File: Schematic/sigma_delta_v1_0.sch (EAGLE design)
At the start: 46 parts, among them IC1 MC78M12CDTG, IC2 MC78M12CDTG, Q1 BS170, Q2 BS170, Q3 BSS84, Q4 BSS84, X1 1751251, X2 1751248, X3 1751264

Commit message: intermediate commit before rework of the input stage
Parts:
- removed IC1: MC78M12CDTG, linear:MC78M12CDTG
- added F3: (no value), rcl:R-EU_M1206
- added IC3: UA78M33DCY, linear:UA78M33DCY
- added J1: SJ1-3523N, SamacSys_Parts:SJ1-3523N
- added JUMPER1, JUMPER2: 0, resistor:R-EU_R0402
- added Q5: BSD223P, transistor-fet:BSD223P
- added R15, R16: 10, eagle-ltspice:RR0603
- C5: device eagle-ltspice:CC3640 -> rcl:C-USC2220K
- D1, D2, D3: value 1N4446 -> (none); device diode:1N4446 -> diode:DIODE-DO214AC
- JP2: device jumper:JP4E -> pinhead:PINHD-1X4_2.54-SMD
- L1: value (none) -> 09HCP-330M-50; device resistor:L-EUTJ5-U2 -> SamacSys_Parts:09HCP-330M-50
- Q3, Q4: value BSS84 -> IRF3707S; device transistor-small-signal:BSS84 -> transistor-power:IRF3704S
- U$2, U$3: device IR2011:IRF3707 -> transistor-power:BUZ11BV
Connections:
- new net N$23: OK2.VO, R16.2
- new net N$24: C5.1, JUMPER1.2, JUMPER2.2, L1.2, X2-2.K
- new net N$25: J1.TIP, JUMPER1.1
- new net N$26: C1.1, D2.C, D3.A, L1.1, Q3.S, Q4.D, R9.2, U$1.VS, U$2.S, U$3.D
- new net N$8: OK1.VO, R15.2
- new net VCC: J1.SLEEVE
- net GND: now also F3.1, IC3.GND, IC3.GND@1, Q4.S, U$3.S; no longer IC1.GND, U$3.D, X1-3.K
- net N$10: now also J1.RING, JUMPER2.1; no longer C5.1, L1.2, X2-2.K
- net N$14: now also Q3.G
- net N$15: now also Q4.G
- net N$19: now also Q5A.D; no longer Q3.D
- net N$21: now also Q5B.D; no longer Q4.D
- net N$22: now also Q5B.G, R16.1; no longer OK2.VO, Q4.G
- net N$7: now also Q5A.G, R15.1; no longer OK1.VO, Q3.G
- net N$9: now also F3.2, X1-3.K; no longer C1.1, D2.C, D3.A, L1.1, R9.2, U$1.VS, U$2.D, U$3.S
- net VCC_12: now also IC3.VI; no longer IC1.VI
- net VCC_3.3: now also IC3.VO, Q5A.S, Q5B.S; no longer IC1.VO, Q3.S, Q4.S
- net VCC_HI: now also Q3.D, U$2.D; no longer U$2.S
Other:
- note added: "Consider placeing temperature sensors"
- note added: "Placment optional"
- note added: "Should be in one package"
- note removed: "Should be in one package or matched!"
- moved on the sheet: C1, C4, C5, R10, R13, R14, R3, R4, R7, R8, R9, X2-1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

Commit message: continued replaceing parts with smd components
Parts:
- removed Q1, Q2: BS170, transistor-small-signal:BS170
- added SJ1: (no value), jumper:SJ2W
- added U$4: BSD235N, SamacSys_Parts:BSD235N
- C1: device eagle-ltspice:CC3640 -> rcl:C-USC2220K
- C10, C9: device rcl:CPOL-EUE2.5-7 -> rcl:CPOL-EUUD-10X10
- C2, C3: device rcl:CPOL-EUE2-5 -> rcl:CPOL-EUUD-6,3X7,7
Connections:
- removed net VCC: J1.SLEEVE
- new net N$27: C11.1, IC2.VI, SJ1.2
- net GND: now also U$4G$1.S, U$4G$2.S; no longer Q1.S, Q2.S
- net N$11: now also U$4G$2.G; no longer Q2.G
- net N$12: now also U$4G$1.G; no longer Q1.G
- net N$3: now also U$4G$1.D; no longer Q1.D
- net N$4: now also U$4G$2.D; no longer Q2.D
- net VCC_HI: now also SJ1.3; no longer C11.1, IC2.VI
- net VCC_MID: now also J1.SLEEVE, SJ1.1
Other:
- note removed: "Should be in one package"
- moved on the sheet: R5

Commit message: finished rework of the Schematic and cleaned up repository
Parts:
- removed JP2: (no value), pinhead:PINHD-1X4_2.54-SMD
- removed OK1, OK2: 6N137, optocoupler:6N137
- removed X3: 1751264, con-phoenix-350:1751264
- added C13, C14: (no value), rcl:C-EUC0603
- added C8: 100n, rcl:C-EUC0603
- added IC1, IC4: LM50, linear:LM50
- added IC5: ACPL-064L-000E, SamacSys_Parts:ACPL-064L-000E
- added JP1: (no value), pinhead:PINHD-2X3_2.54
- added R17, R18: 10, eagle-ltspice:RR0603
- added X4: 1751280, con-phoenix-350:1751280
- C11, C6: value (none) -> 330n
- C12, C7: value (none) -> 100n
- R1, R2: value 270 -> 1k
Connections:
- net N$26 renamed H_BRIDGE_MID
- new net N$26: IC5.VO1, R15.2
- new net N$28: C13.1, JP1.1, R17.1, X4-1.K
- new net N$29: C14.1, JP1.5, R18.1, X4-5.K
- new net N$32: IC1.VO, R18.2
- net GND: now also C13.2, C14.2, C8.2, IC1.GND, IC4.GND, IC5.GND, JP1.6, X4-6.K; no longer JP2.1, OK1.GND, OK2.GND, X3-1.K
- net N$1: now also JP1.3, X4-3.K; no longer JP2.4, X3-4.K
- net N$2: now also JP1.4, X4-4.K; no longer JP2.3, X3-3.K
- net N$23: now also IC4.VO, R17.2; no longer OK2.VO, R16.2
- net N$3: now also IC5.CATHODE1; no longer OK1.C
- net N$4: now also IC5.CATHODE2; no longer OK2.C
- net N$5: now also IC5.ANODE1; no longer OK1.A
- net N$6: now also IC5.ANODE2; no longer OK2.A
- net N$8: now also IC5.VO2, R16.2; no longer OK1.VO, R15.2
- net VCC_3.3: now also C8.1, IC1.+VS, IC4.+VS, IC5.VDD; no longer OK1.VCC, OK1.VE, OK2.VCC, OK2.VE
- net VCC_FPGA: now also JP1.2, X4-2.K; no longer JP2.2, X3-2.K
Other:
- note added: "Place near output transistors"
- note removed: "Consider placeing temperature sensors"
- moved on the sheet: C5, D2, D3, J1, JUMPER1, JUMPER2, L1, Q3, Q4, Q5A, Q5B, R1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

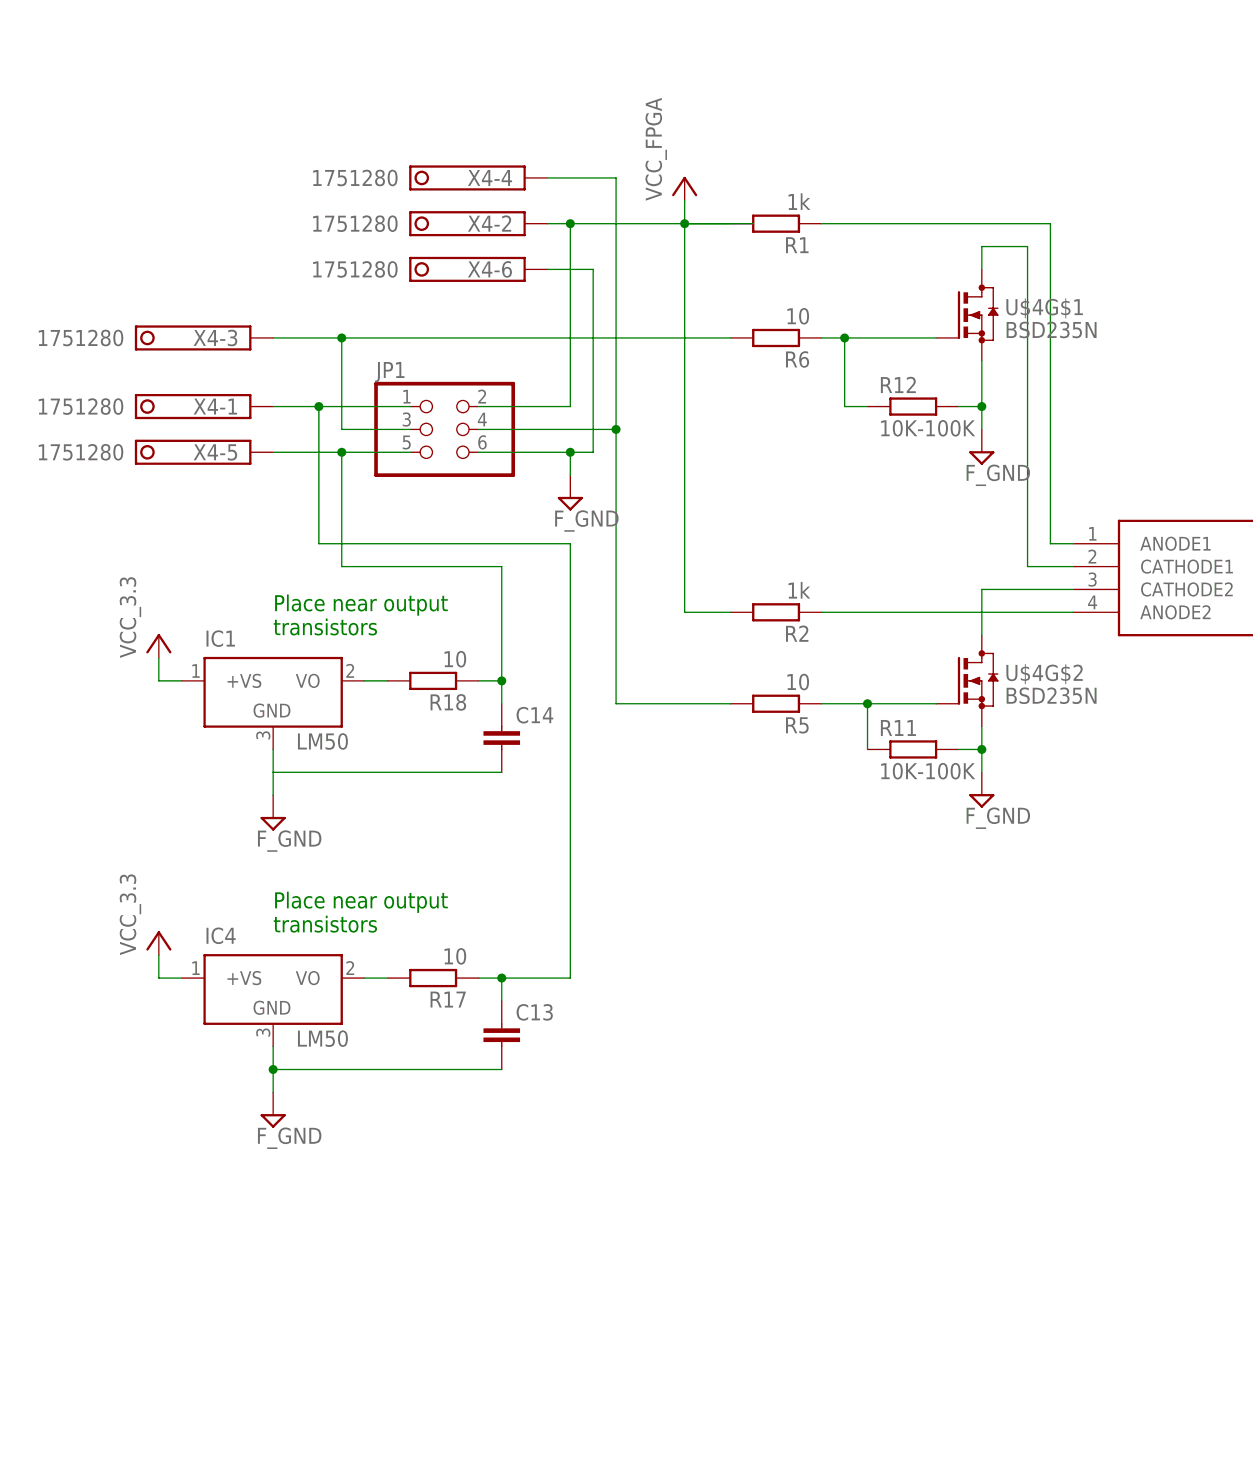
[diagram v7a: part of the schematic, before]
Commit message: continued layouting and added analog decoupling for temperature sensors
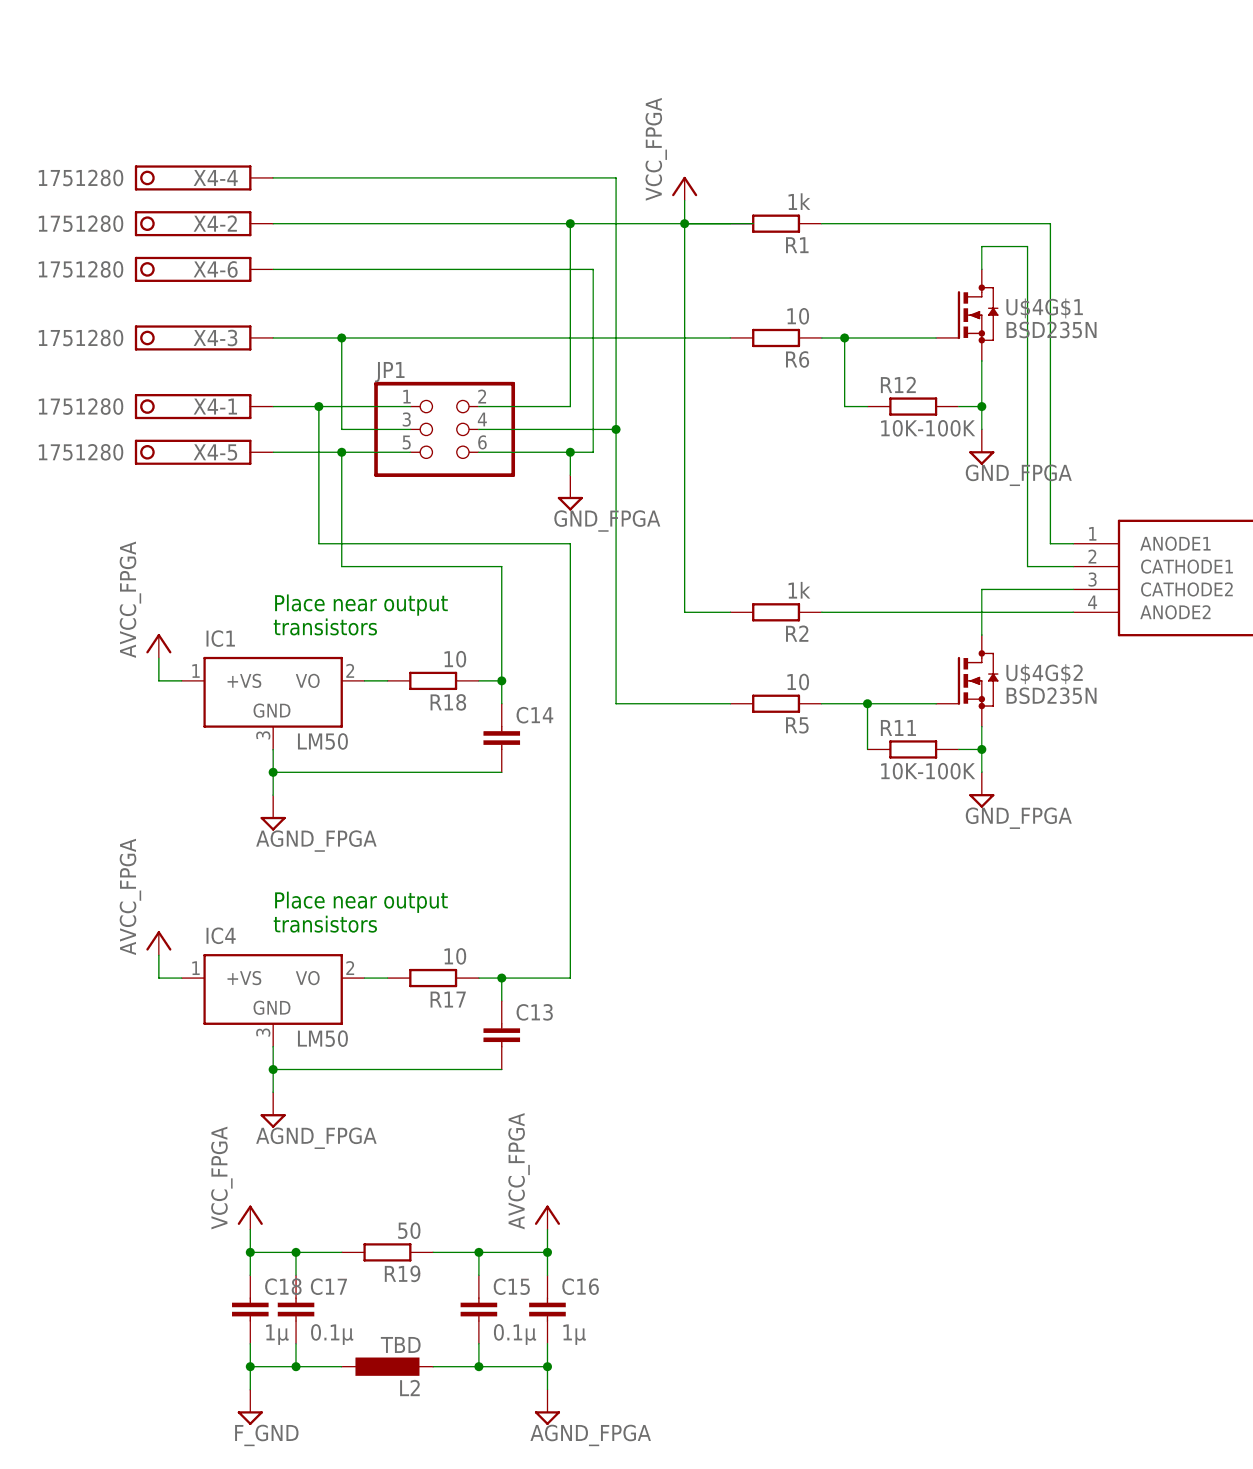
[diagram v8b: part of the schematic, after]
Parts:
- added C15, C17: 0.1µ, rcl:C-EUC0603
- added C16, C18: 1µ, rcl:C-EUC0603
- added L2: TBD, rcl:L-EUL2012C
- added R19: 50, eagle-ltspice:RR0603
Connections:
- new net AGND_FPGA: C13.2, C14.2, C15.2, C16.2, IC1.GND, IC4.GND, L2.2
- new net AVCC_FPGA: C15.1, C16.1, IC1.+VS, IC4.+VS, R19.1
- new net GND_FPGA: JP1.6, R11.2, R12.2, U$4G$1.S, U$4G$2.S, X4-6.K
- net GND: now also C17.2, C18.2, L2.1; no longer C13.2, C14.2, IC1.GND, IC4.GND, JP1.6, R11.2, R12.2, U$4G$1.S, U$4G$2.S, X4-6.K
- net VCC_3.3: no longer IC1.+VS, IC4.+VS
- net VCC_FPGA: now also C17.1, C18.1, R19.2
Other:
- moved on the sheet: X4-2, X4-4, X4-6
